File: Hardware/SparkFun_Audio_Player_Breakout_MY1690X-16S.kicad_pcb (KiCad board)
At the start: 4 copper layers, 25.4 x 25.4 mm, 70 parts, among them J1 3.5mm TRRS, J2 Conn_01x03, J3 Conn_01x02, J4 USB_C_Receptacle, J5 Conn_01x06, J6 microSD, Q1 BSS138, U2 MY1690X-16S

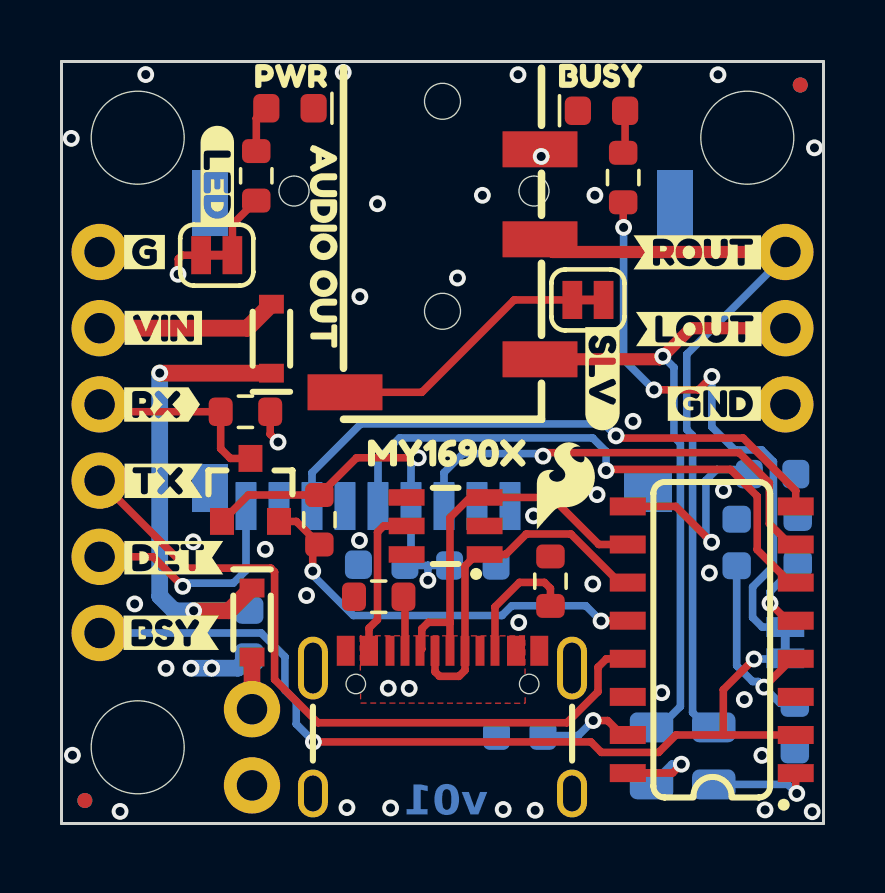
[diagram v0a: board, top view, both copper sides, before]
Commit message: Post-proto testing changes - v10
-bumped version to v10 in sch and brd
-added 3.4-5V in buzzard labels at the header pin
-added over-bar to sd detect silk
-added pullup resistor on sd detect
-Move 3.3V_P trace elsewhere to avoid coupling and keep a complete plane (VCC) under the USB D+/D- lines.
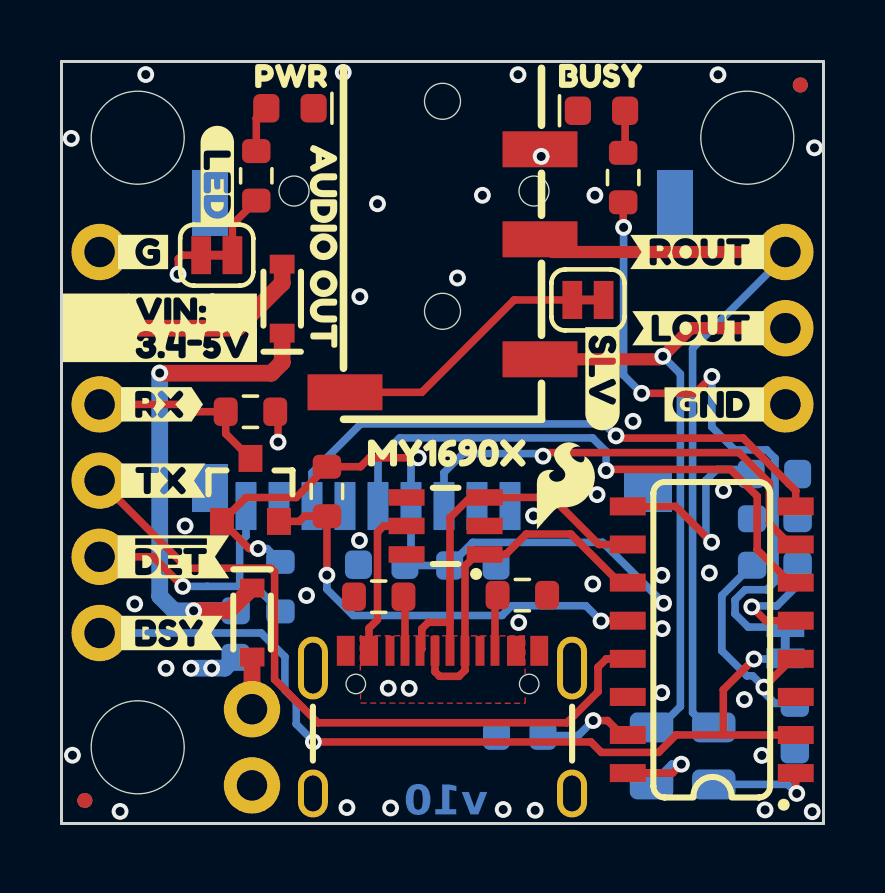
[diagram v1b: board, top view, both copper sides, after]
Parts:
- removed kibuzzard-6792C82F: G***, kibuzzard-6792C82F
- removed kibuzzard-6792C85C: G***, kibuzzard-6792C85C
- removed the kibuzzard-6792C876 at (137.4, 97.8)
- removed kibuzzard-6792C889: G***, kibuzzard-6792C889
- removed kibuzzard-6792C89C: G***, kibuzzard-6792C89C
- removed kibuzzard-6792C8F2: G***, kibuzzard-6792C8F2
- removed kibuzzard-6792C902: G***, kibuzzard-6792C902
- removed kibuzzard-6792C9C9: G***, kibuzzard-6792C9C9
- removed kibuzzard-6792CBB2: G***, kibuzzard-6792CBB2
- removed kibuzzard-6792CC46: G***, kibuzzard-6792CC46
- removed kibuzzard-6793B9F5: G***, kibuzzard-6793B9F5
- removed kibuzzard-679A5CF8: G***, kibuzzard-679A5CF8
- added G***: Flame, SparkFun-Aesthetic:SparkFun_Flame_3mm, B.Cu at (153.3, 108.5)
- added R6: 100k, SparkFun-Resistor:R_0603_1608Metric, B.Cu at (141.9, 108.9)
- added kibuzzard-6792C7DD: G***, kibuzzard-6792C7DD, B.Cu at (147.1, 109.6)
- added kibuzzard-67AD02A2: G***, kibuzzard-67AD02A2, F.Cu at (139.0, 100.9)
- added kibuzzard-67AD02AA: G***, kibuzzard-67AD02AA, F.Cu at (138.3, 99.7)
- added kibuzzard-67AD03CF: G***, kibuzzard-67AD03CF, B.Cu at (138.3, 100.8)
- added kibuzzard-67AD03ED: G***, kibuzzard-67AD03ED, B.Cu at (138.1, 99.7)
- added kibuzzard-67B388A6: G***, kibuzzard-67B388A6, F.Cu at (137.3, 97.8)
- added kibuzzard-67B38923: G***, kibuzzard-67B38923, F.Cu at (138.0, 102.9)
- added kibuzzard-67B391D1: G***, kibuzzard-67B391D1, F.Cu at (138.0, 105.4)
- added kibuzzard-67B391E8: G***, kibuzzard-67B391E8, F.Cu at (138.3, 108.0)
- added kibuzzard-67B3920A: G***, kibuzzard-67B3920A, F.Cu at (138.3, 110.5)
- added kibuzzard-67B39233: G***, kibuzzard-67B39233, F.Cu at (155.8, 97.8)
- added kibuzzard-67B39251: G***, kibuzzard-67B39251, F.Cu at (155.8, 100.3)
- added kibuzzard-67B39267: G***, kibuzzard-67B39267, F.Cu at (156.4, 102.9)
- added kibuzzard-67B394D8: G***, kibuzzard-67B394D8, B.Cu at (138.4, 108.0)
- moved D2 1.38 mm to (142.0, 99.3)
- moved R2 1.05 mm to (150.0, 109.2), turned to 0 degrees
- moved R1 0.98 mm to (143.5, 105.8)
- moved C9 0.52 mm to (157.6, 107.5)
- moved L1 0.45 mm to (140.4, 110.5)
- moved R4 0.17 mm to (140.9, 103.1)
- moved C7 0.06 mm to (158.4, 105.2)
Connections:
- net SD_DET renamed ~{SD_DET}
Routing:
- net ~{SD_DET}: track 7.65 -> 10.1 mm
- net Net-(J4-CC2): track 4.32 -> 1.89 mm
- net 3.3V_P: track 28.5 -> 30.7 mm, vias 3 -> 4
- net Net-(JP1-A): track 19.7 -> 21.4 mm
- net VIN: track 6.06 -> 7.34 mm
- net Net-(D2-K): track 16.6 -> 17.7 mm
- net MY_RX_LV: track 14.2 -> 14.8 mm
- net GND: vias 36 -> 37
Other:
- board text added: "v10"
- board text removed: "v01"

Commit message: checklist reds eng v10
-update measures
-update kicad layer naming to new standards
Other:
- board text removed: "NPTH (NON PLATED THROUGH HOLE) Drills: 1.2mm dia (0.0472 inch dia) ALL OTHER DRILLS PLATED THROUGH HOLE"

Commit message: soldermask color RED
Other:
- board text added: "Solder Mask: Red"
- board text removed: "Solder Mask: Black"
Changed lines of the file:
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@@
 		)
 	)
-	(gr_text "Solder Mask: Black"
+	(gr_text "Solder Mask: Red"
 		(at 189.019 140.231 0)
 		(layer "Eco1.User")
